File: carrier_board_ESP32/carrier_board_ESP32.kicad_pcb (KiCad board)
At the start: 4 copper layers, 45 parts, among them IC1 SS49E, IC2 SS49E, IC3 SS49E, IC4 SS49E, IC5 SS49E, IC6 SS49E, IC7 DRV5023, IC8 DRV5023, J1 BME280, J2 LTR390, J3 ENS160 I2C, J4 ENS160 SPI, J5 ENS160 + AHT21, J6 Conn_01x02_Socket, J7 Conn_01x02_Socket, J8 UJC-HP-3-SMT-TR, U1 ESP32-S3-DEVKITC-1-N8R2, U2 TP4056, U3 LM2576HVS-5, U4 MT3608

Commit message: pcb changes
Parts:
- removed C7, C8: 0.01uF, Capacitor_SMD:C_0805_2012Metric_Pad1.18x1.45mm_HandSolder
- removed D3, D4: DO-214AC, Diode_SMD:D_SMA_Handsoldering
- removed IC1, IC2, IC3, IC4, IC5, IC6: SS49E, SS49F:TO130P160X410X300-3P
- removed IC7, IC8: DRV5023, SS49F:TO130P160X410X300-3P
- removed J4: ENS160 SPI, Connector_PinHeader_2.54mm:PinHeader_1x07_P2.54mm_Vertical
- removed J5: ENS160 + AHT21, Connector_PinHeader_2.54mm:PinHeader_1x08_P2.54mm_Vertical
- removed J6, J7: Conn_01x02_Socket, Connector_AMASS:AMASS_XT30UPB-F_1x02_P5.0mm_Vertical
- removed J8: UJC-HP-3-SMT-TR, UJC-HP-3-SMT-TR:CUI_UJC-HP-3-SMT-TR
- added CHRG1: RED, LED_SMD:LED_0805_2012Metric_Pad1.15x1.40mm_HandSolder, F.Cu at (198.1, 97.7)
- added DIR1: Conn_01x03_Socket, Connector_PinHeader_2.54mm:PinHeader_1x03_P2.54mm_Vertical, F.Cu at (183.5, 27.0)
- added DIR2: Conn_01x03_Socket, Connector_PinHeader_2.54mm:PinHeader_1x03_P2.54mm_Vertical, F.Cu at (183.5, 31.5)
- added DIR3: Conn_01x03_Socket, Connector_PinHeader_2.54mm:PinHeader_1x03_P2.54mm_Vertical, F.Cu at (183.5, 36.0)
- added DIR4: Conn_01x03_Socket, Connector_PinHeader_2.54mm:PinHeader_1x03_P2.54mm_Vertical, F.Cu at (183.5, 40.5)
- added DIR5: Conn_01x03_Socket, Connector_PinHeader_2.54mm:PinHeader_1x03_P2.54mm_Vertical, F.Cu at (183.5, 45.0)
- added DIR6: Conn_01x03_Socket, Connector_PinHeader_2.54mm:PinHeader_1x03_P2.54mm_Vertical, F.Cu at (183.5, 49.5)
- added J12: LTR390, Connector_PinHeader_2.54mm:PinHeader_1x06_P2.54mm_Vertical, F.Cu at (184.3, 77.0)
- added J13: BME280, Connector_PinHeader_2.54mm:PinHeader_1x06_P2.54mm_Vertical, F.Cu at (184.3, 70.5)
- added J14: ENS160 SPI, Connector_PinHeader_2.54mm:PinHeader_1x07_P2.54mm_Vertical, F.Cu at (184.4, 90.0)
- added J15: ENS160 + AHT21, Connector_PinHeader_2.54mm:PinHeader_1x08_P2.54mm_Vertical, F.Cu at (184.3, 83.5)
- added J16: ENS160 I2C, Connector_PinHeader_2.54mm:PinHeader_1x04_P2.54mm_Vertical, F.Cu at (184.5, 64.0)
- added J17: Conn_01x22_Socket, Connector_PinHeader_2.54mm:PinHeader_1x22_P2.54mm_Vertical, F.Cu at (211.0, 33.9)
- added J18: Conn_01x22_Socket, Connector_PinHeader_2.54mm:PinHeader_1x22_P2.54mm_Vertical, F.Cu at (245.5, 33.9)
- added R11: 2kΩ, Resistor_SMD:R_0805_2012Metric_Pad1.20x1.40mm_HandSolder, F.Cu at (265.9, 42.5)
- added R12: 4k7Ω, Resistor_SMD:R_0805_2012Metric_Pad1.20x1.40mm_HandSolder, F.Cu at (269.4, 32.0)
- added R13: 1kΩ, Resistor_SMD:R_0805_2012Metric_Pad1.20x1.40mm_HandSolder, F.Cu at (269.9, 37.0)
- added R14: 2kΩ, Resistor_SMD:R_0805_2012Metric_Pad1.20x1.40mm_HandSolder, F.Cu at (265.9, 37.0)
- added SPEED1: Conn_01x03_Socket, Connector_PinHeader_2.54mm:PinHeader_1x03_P2.54mm_Vertical, F.Cu at (273.9, 31.0)
- added SPEED2: Conn_01x03_Socket, Connector_PinHeader_2.54mm:PinHeader_1x03_P2.54mm_Vertical, F.Cu at (273.9, 48.5)
- added STDBY1: GREEN, LED_SMD:LED_0805_2012Metric_Pad1.15x1.40mm_HandSolder, F.Cu at (198.1, 102.2)
- C3: value 100nF -> 1000uF; footprint Capacitor_SMD:C_0805_2012Metric_Pad1.18x1.45mm_HandSolder -> Capacitor_SMD:C_Elec_10x10.2
- C4: value 1000uF -> 22nF
- C6: value 22nF -> 100nF
- D1: value GREEN -> DO-214AC; footprint LED_SMD:LED_0805_2012Metric_Pad1.15x1.40mm_HandSolder -> Diode_SMD:D_SMA_Handsoldering
- D2: value RED -> DO-214AC; footprint LED_SMD:LED_0805_2012Metric_Pad1.15x1.40mm_HandSolder -> Diode_SMD:D_SMA_Handsoldering
- J1: value BME280 -> Conn_01x02_Socket; footprint Connector_PinHeader_2.54mm:PinHeader_1x06_P2.54mm_Vertical -> Connector_AMASS:AMASS_XT30PW-M_1x02_P2.50mm_Horizontal
- J2: value LTR390 -> Conn_01x02_Socket; footprint Connector_PinHeader_2.54mm:PinHeader_1x06_P2.54mm_Vertical -> Connector_AMASS:AMASS_XT30PW-M_1x02_P2.50mm_Horizontal
- J3: value ENS160 I2C -> UJC-HP-3-SMT-TR; footprint Connector_PinHeader_2.54mm:PinHeader_1x04_P2.54mm_Vertical -> UJC-HP-3-SMT-TR:CUI_UJC-HP-3-SMT-TR
- R1: value 1kΩ -> 0.4Ω
- R10: value 10kΩ -> 1kΩ
- R3: value 0.4Ω -> 1kΩ
- R4: value 330Ω -> 110kΩ
- R5: value 5.1kΩ -> 15kΩ
- R6: value 5.1kΩ -> 330Ω
- R7: value 110kΩ -> 5.1kΩ
- R8: value 15kΩ -> 5.1kΩ
- R9: value 10kΩ -> 4k7Ω
- U1: value ESP32-S3-DEVKITC-1-N8R2 -> TP4056; footprint ESP32-S3-DEVKITC-1-N8R2:XCVR_ESP32-S3-DEVKITC-1-N8R2 -> TP4056:SOP127P600X175-9N
- U2: value TP4056 -> LM2576HVS-5; footprint TP4056:SOP127P600X175-9N -> Package_TO_SOT_SMD:TO-263-5_TabPin3
- U3: value LM2576HVS-5 -> MT3608; footprint Package_TO_SOT_SMD:TO-263-5_TabPin3 -> Package_TO_SOT_SMD:SOT-23-6
- U4: value MT3608 -> ESP32-S3-DEVKITC-1-N8R2; footprint Package_TO_SOT_SMD:SOT-23-6 -> ESP32-S3-DEVKITC-1-N8R2:XCVR_ESP32-S3-DEVKITC-1-N8R2
- moved J2 252.6 mm to (273.0, 110.0), turned to -90 degrees
- moved C3 243.7 mm to (261.0, 99.3), turned to 180 degrees
- moved C4 236.0 mm to (250.6, 107.0)
- moved L1 232.9 mm to (264.5, 89.3), turned to 180 degrees
- moved C5 230.6 mm to (242.5, 114.5), turned to -90 degrees
- moved R5 222.7 mm to (247.6, 114.5), turned to -90 degrees
- moved U2 221.5 mm to (262.5, 111.9), turned to -90 degrees
- moved R4 221.3 mm to (247.6, 108.5), turned to -90 degrees
- moved D1 220.7 mm to (268.0, 98.3)
- moved R9 219.0 mm to (269.4, 47.5), turned to 90 degrees
- moved R10 218.1 mm to (269.9, 42.5), turned to 180 degrees
- moved L2 205.9 mm to (234.5, 112.0), turned to 90 degrees
- moved C6 202.4 mm to (212.0, 115.0), turned to 90 degrees
- moved U3 200.9 mm to (244.5, 110.5), turned to 180 degrees
- moved R8 198.6 mm to (221.2, 111.5)
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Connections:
- C1 pad 1: Net-(D1-A) -> Net-(CHRG1-A)
- C3 pad 1: Net-(C3-Pad1) -> /5V_supply
- C4 pad 1: /5V_supply -> /5V
- C6 pad 1: /5V -> Net-(C6-Pad1)
- D1 pad 2: Net-(D1-A) -> GND
- D2 pad 1: Net-(D2-K) -> /5V
- D2 pad 2: Net-(D1-A) -> Net-(D2-A)
- J1 pad 1: /VCC -> GND
- J1 pad 2: GND -> /BATT+
- J2 pad 1: /VIN -> GND
- J2 pad 2: /3V3 -> /SOLAR+
- L1 pad 1: Net-(D3-K) -> Net-(D1-K)
- L2 pad 2: Net-(D4-A) -> Net-(D2-A)
- R1 pad 1: Net-(D1-K) -> /5V_supply
- R1 pad 2: Net-(U2-~{STDBY}) -> Net-(CHRG1-A)
- R10 pad 1: /3V3 -> /OUT2
- R2 pad 1: Net-(D2-K) -> Net-(STDBY1-K)
- R2 pad 2: Net-(U2-~{CHRG}) -> Net-(U1-~{STDBY})
- R3 pad 1: /5V_supply -> Net-(CHRG1-K)
- R3 pad 2: Net-(D1-A) -> Net-(U1-~{CHRG})
- R4 pad 1: Net-(C3-Pad1) -> /5V
- R4 pad 2: GND -> Net-(U3-FB)
- R5 pad 1: Net-(J8-CC2) -> Net-(U3-FB)
- R6 pad 1: Net-(J8-CC1) -> Net-(C6-Pad1)
- R7 pad 1: /5V -> Net-(J3-CC1)
- R7 pad 2: Net-(U4-FB) -> GND
- R8 pad 1: Net-(U4-FB) -> Net-(J3-CC2)
- R9 pad 1: /3V3 -> /5V
- R9 pad 2: /SPEED_1 -> /OUT2
- Rprog1 pad 1: Net-(U2-PROG) -> Net-(U1-PROG)
- U2 pad 1: GND -> /SOLAR+
- U2 pad 2: Net-(U2-PROG) -> Net-(D1-K)
- U2 pad 4: Net-(D1-A) -> /5V_supply
- U2 pad 5: /BATT+ -> GND
- U3 pad 1: /SOLAR+ -> Net-(D2-A)
- U3 pad 2: Net-(D3-K) -> GND
- U3 pad 3: GND -> Net-(U3-FB)
- U3 pad 4: /5V_supply -> GND
- U3 pad 5: GND -> /5V_supply
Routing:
- net /5V: track 0.00 -> 217.2 mm
- net /3V3: track 0.00 -> 104.6 mm, vias 0 -> 2
- net /5V_supply: track 0.00 -> 100.4 mm, vias 0 -> 3
- net /SCL: track 0.00 -> 43.6 mm, vias 0 -> 1
- net /SDA: track 0.00 -> 40.0 mm, vias 0 -> 1
- net /SCK: track 0.00 -> 36.2 mm, vias 0 -> 1
- net /MISO: track 0.00 -> 36.2 mm
- net /CS_3: track 0.00 -> 35.3 mm
- net /CS_1: track 0.00 -> 35.0 mm
- net /DIR_1: track 0.00 -> 34.5 mm
- net /MOSI: track 0.00 -> 34.2 mm, vias 0 -> 1
- net /DIR_2: track 0.00 -> 33.7 mm
- net /DIR_3: track 0.00 -> 32.9 mm
- net /DIR_4: track 0.00 -> 32.1 mm
- net Net-(CHRG1-A): track 0.00 -> 31.8 mm, vias 0 -> 2
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- added copper zone on B.Cu, net GND
- added copper zone on F.Cu, net GND
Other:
- board outline added: 100 x 100 mm
- board text added: "${CURRENT_DATE}"
- board text added: "${TITLE} ${COMMENT2}"
- board text added: "3V3"
- board text added: "3Vo"
- board text added: "5V Boost Converter"
- board text added: "5V Step-Down Converter"
- board text added: "5V|GND|DIR"
- board text added: "5V|GND|OUT"
- board text added: "ADD"
- board text added: "Adam Prystupa"
- board text added: "BME280"
- board text added: "Battery Charging Circuit"
- board text added: "CS"
- board text added: "CSB"
- board text added: "Carrier Board ESP32-S3"
- board text added: "ENS160 + AHT21"
- board text added: "ENS160 I2C"
- board text added: "ENS160 SPI"
- board text added: "ESP32-S3 Core"
- board text added: "GND"
- board text added: "Hall Sensors Connectors (Wind Direction)"
- board text added: "Hall Sensors Connectors (Wind Speed)"
- board text added: "INT"
- board text added: "LTR390"
- board text added: "OUT|GND|5V"
- board text added: "PROJECT Rev. 1.0"
- board text added: "Project author:"
- board text added: "Project info:"
- board text added: "SCK"
- board text added: "SCL"
- board text added: "SDA"
- board text added: "SDI"
- board text added: "SDO"
- board text added: "Sensor Header"
- board text added: "USB Power Input + Protection"
- board text added: "VCC"
- board text added: "VIN"

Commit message: updated scheme and PCB ready for inspection
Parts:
- added C10: 10uF, Capacitor_SMD:C_0805_2012Metric_Pad1.18x1.45mm_HandSolder, F.Cu at (263.0, 98.2)
- added C11: 47uF, Capacitor_SMD:C_0805_2012Metric_Pad1.18x1.45mm_HandSolder, F.Cu at (246.8, 115.8)
- added C12: 2200uF, Capacitor_SMD:CP_Elec_10x10.5, F.Cu at (240.2, 104.0)
- added C13: 10uF, Capacitor_Tantalum_SMD:CP_EIA-7343-15_Kemet-W_Pad2.25x2.55mm_HandSolder, F.Cu at (210.7, 107.6)
- added C14: 1uF, Capacitor_SMD:C_0805_2012Metric_Pad1.18x1.45mm_HandSolder, F.Cu at (208.2, 111.6)
- added C15: 10uF, Capacitor_SMD:C_0805_2012Metric_Pad1.18x1.45mm_HandSolder, F.Cu at (239.2, 115.8)
- added C16: 10uF, Capacitor_SMD:C_0805_2012Metric_Pad1.18x1.45mm_HandSolder, F.Cu at (241.8, 115.8)
- added C17: 10uF, Capacitor_SMD:C_0805_2012Metric_Pad1.18x1.45mm_HandSolder, F.Cu at (244.2, 115.8)
- added C7: 100uF, Capacitor_Tantalum_SMD:CP_EIA-7343-15_Kemet-W_Pad2.25x2.55mm_HandSolder, F.Cu at (256.0, 77.8)
- added C8: 10uF, Capacitor_SMD:C_0805_2012Metric_Pad1.18x1.45mm_HandSolder, F.Cu at (258.2, 82.8)
- added C9: 100uF, Capacitor_Tantalum_SMD:CP_EIA-7343-15_Kemet-W_Pad2.25x2.55mm_HandSolder, F.Cu at (265.8, 102.0)
- moved C3 34.4 mm to (230.5, 115.2)
- moved L2 31.3 mm to (265.8, 112.5), turned to -90 degrees
- moved J2 31.0 mm to (264.4, 80.2)
- moved D2 23.9 mm to (257.0, 114.5), turned to 90 degrees
- moved U2 22.6 mm to (271.1, 91.0), turned to 0 degrees
- moved D1 16.7 mm to (254.7, 88.2), turned to 180 degrees
- moved L1 13.0 mm to (254.2, 97.2), turned to -90 degrees
- moved C4 8.86 mm to (249.2, 115.8), turned to 90 degrees
- moved C5 8.50 mm to (247.2, 107.5), turned to 90 degrees
- moved R4 8.34 mm to (251.8, 115.8), turned to 90 degrees
- moved R5 6.38 mm to (254.0, 114.0), turned to 90 degrees
- moved C2 5.94 mm to (194.6, 102.7)
- moved J1 5.00 mm to (190.0, 107.5)
- moved U3 4.18 mm to (248.5, 111.8)
- moved J12 4.03 mm to (183.8, 73.0)
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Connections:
- C3 pad 1: /5V_supply -> /5V
- J18 pad 17: /GPIO47 -> /5V
- J18 pad 18: /GPIO21 -> /5V
- J18 pad 19: /GPIO20 -> /5V
- J18 pad 20: /GPIO19 -> /5V
- J18 pad 21: GND -> /5V
- J18 pad 22: GND -> /5V
- U4 pad J3_17: /GPIO47 -> /5V
- U4 pad J3_18: /GPIO21 -> /5V
- U4 pad J3_19: /GPIO20 -> /5V
- U4 pad J3_20: /GPIO19 -> /5V
- U4 pad J3_22: GND -> /5V
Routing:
- net /5V: track 217.2 -> 328.3 mm
- net /5V_supply: track 100.4 -> 134.4 mm, vias 3 -> 4
- net /MISO: track 36.2 -> 28.2 mm
- net /GPIO21: track 5.57 -> 0.00 mm
- net /GPIO20: track 5.57 -> 0.00 mm
- net /GPIO19: track 5.57 -> 0.00 mm
- net /GPIO47: track 5.57 -> 0.00 mm
- net Net-(D1-K): track 17.2 -> 11.9 mm
- net /BATT+: track 4.66 -> 9.85 mm
- net /3V3: track 104.6 -> 100.1 mm, vias 2 -> 1
- net /SOLAR+: track 13.7 -> 17.9 mm
- net /INT_3: track 29.3 -> 26.0 mm
- net /SCK: track 36.2 -> 33.1 mm, vias 1 -> 0
- net /MOSI: track 34.2 -> 31.2 mm
- net Net-(CHRG1-A): track 31.8 -> 28.9 mm, vias 2 -> 4
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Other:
- board outline removed

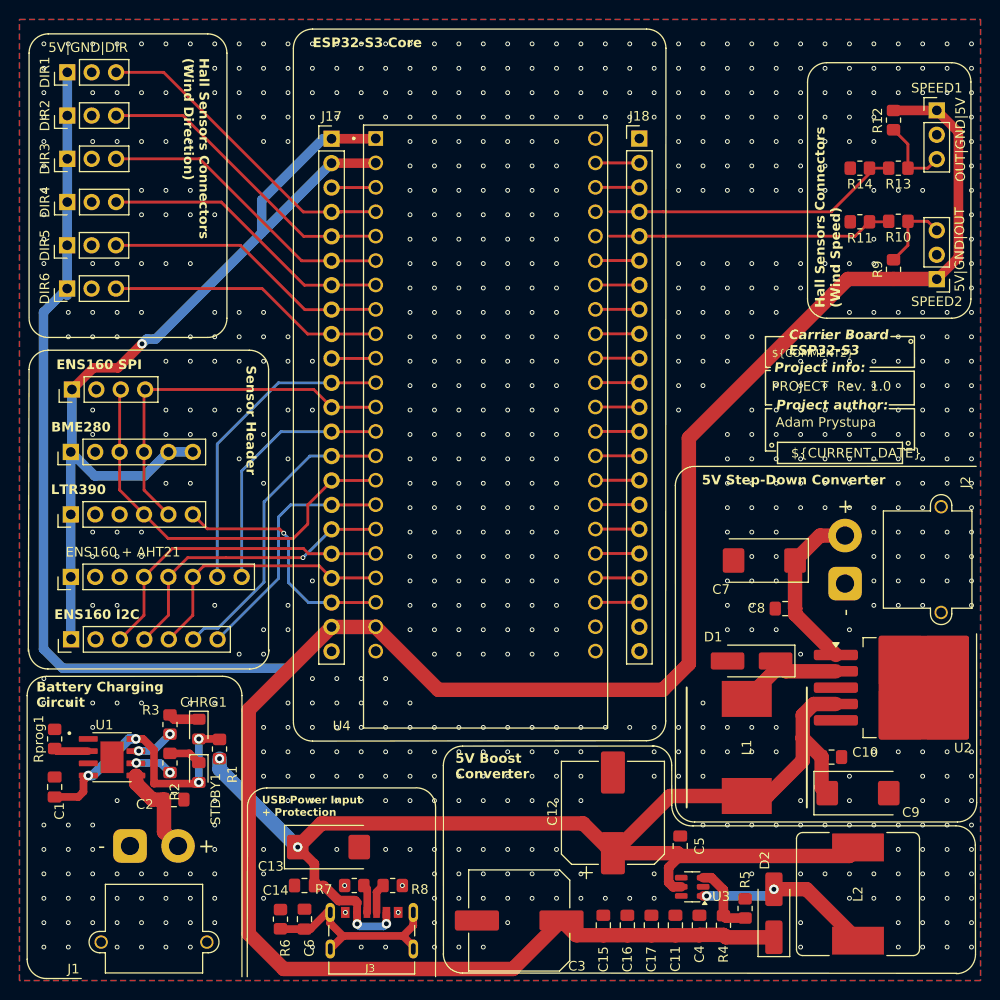
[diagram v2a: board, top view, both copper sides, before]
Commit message: Fixed errors, added mounting holes
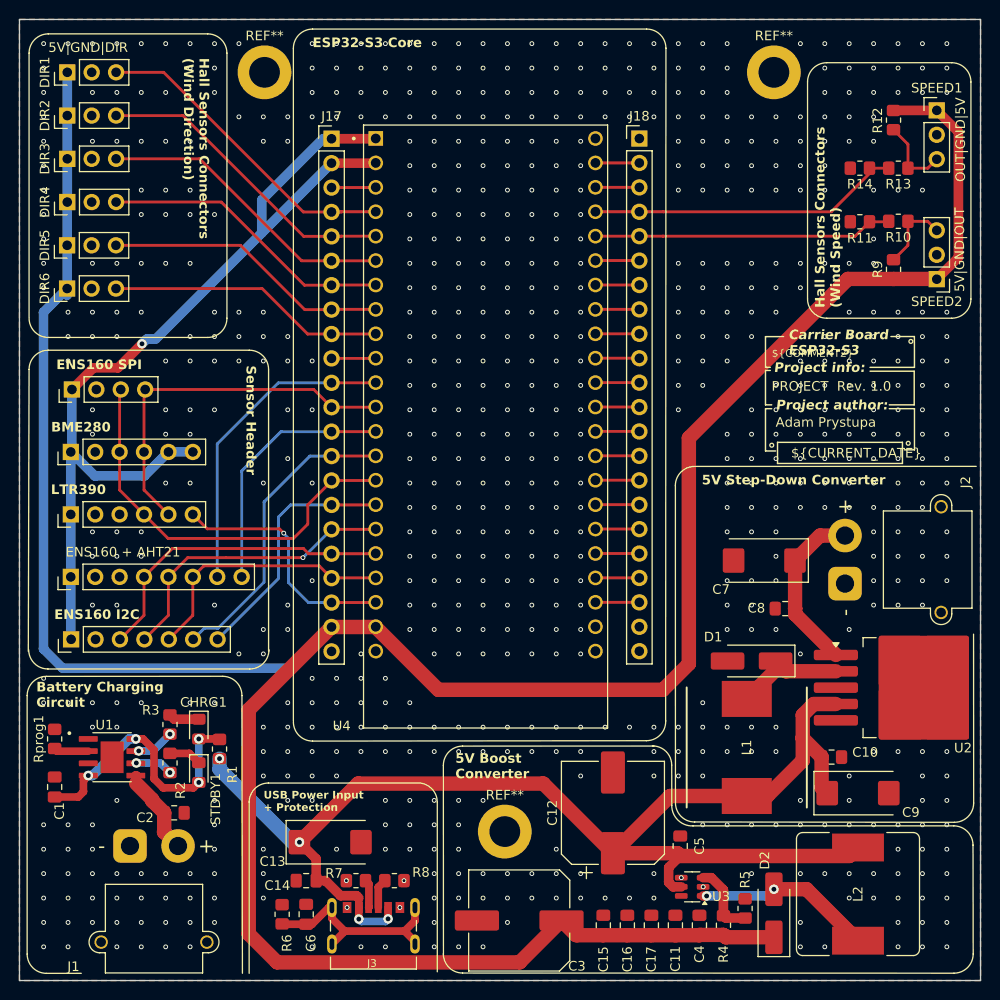
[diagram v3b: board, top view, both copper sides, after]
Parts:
- added REF**: MountingHole_3.2mm_M3_DIN965_Pad, MountingHole:MountingHole_3.2mm_M3_DIN965_Pad, F.Cu at (229.0, 106.0)
- added REF**: MountingHole_3.2mm_M3_DIN965_Pad, MountingHole:MountingHole_3.2mm_M3_DIN965_Pad, F.Cu at (257.0, 27.0)
- added REF**: MountingHole_3.2mm_M3_DIN965_Pad, MountingHole:MountingHole_3.2mm_M3_DIN965_Pad, F.Cu at (204.0, 27.0)
- moved C2 1.38 mm to (194.6, 104.0)
- moved C13 0.54 mm to (210.8, 107.1)
- moved C14 0.54 mm to (208.3, 111.1)
- moved C6 0.54 mm to (208.3, 114.6)
- moved J3 0.54 mm to (215.3, 113.9)
- moved R6 0.54 mm to (205.8, 114.6)
- moved R7 0.54 mm to (213.5, 111.1)
- moved R8 0.54 mm to (217.5, 111.1)
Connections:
- J18 pad 17: /5V -> /GPIO47
- J18 pad 18: /5V -> /GPIO21
- J18 pad 19: /5V -> /GPIO20
- J18 pad 20: /5V -> /GPIO19
- J18 pad 21: /5V -> GND
- J18 pad 22: /5V -> GND
- U4 pad J3_17: /5V -> /GPIO47
- U4 pad J3_18: /5V -> /GPIO21
- U4 pad J3_19: /5V -> /GPIO20
- U4 pad J3_20: /5V -> /GPIO19
- U4 pad J3_22: /5V -> GND
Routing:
- net /5V: track 328.3 -> 309.4 mm
- net /GPIO21: track 0.00 -> 4.57 mm
- net /GPIO20: track 0.00 -> 4.57 mm
- net /GPIO19: track 0.00 -> 4.57 mm
- net /GPIO47: track 0.00 -> 4.57 mm
- net /5V_supply: track 134.4 -> 137.5 mm
- net /SPEED_1: track 31.3 -> 32.7 mm
- net /SPEED_2: track 29.9 -> 31.4 mm
- net /BATT+: track 9.85 -> 9.16 mm
- net GND: vias 782 -> 743
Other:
- board outline added: 100 x 100 mm

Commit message: added step model of pcb
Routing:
- net /CS_3: track 32.5 -> 34.0 mm
- net /INT_1: track 26.7 -> 27.9 mm
- net GND: vias 743 -> 744

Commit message: Ready to fabrication
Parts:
- moved C1 1.17 mm to (181.0, 101.5)
- moved Rprog1 1.17 mm to (181.0, 96.5)
- moved U1 1.16 mm to (187.0, 98.3)
- moved R2 0.63 mm to (194.2, 99.5), turned to 90 degrees
- moved U3 0.50 mm to (248.0, 111.8)
- turned STDBY1 to 90 degrees
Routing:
- net /5V_supply: track 137.5 -> 140.2 mm
- net Net-(D2-A): track 18.6 -> 21.1 mm
- net Net-(U1-~{CHRG}): track 4.28 -> 5.44 mm, vias 2 -> 0
- net Net-(U1-~{STDBY}): track 3.98 -> 4.91 mm, vias 2 -> 0
- net Net-(U3-FB): track 7.68 -> 8.36 mm
- net /BATT+: track 9.16 -> 9.79 mm
- net Net-(CHRG1-A): track 29.0 -> 29.3 mm, vias 4 -> 3
- net GND: vias 744 -> 740

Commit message: cleaning repo
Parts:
- added D3: D, Diode_SMD:D_SMA, F.Cu at (199.0, 105.5)
- moved J1 3.44 mm to (186.6, 107.3)
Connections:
- U3 pad 4: GND -> /5V_supply
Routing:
- net /BATT+: track 9.79 -> 16.2 mm
- net /5V_supply: track 140.2 -> 145.8 mm
- net GND: vias 740 -> 734
